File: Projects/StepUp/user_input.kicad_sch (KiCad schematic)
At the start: 3 parts, among them J15 Conn_02x03_Odd_Even

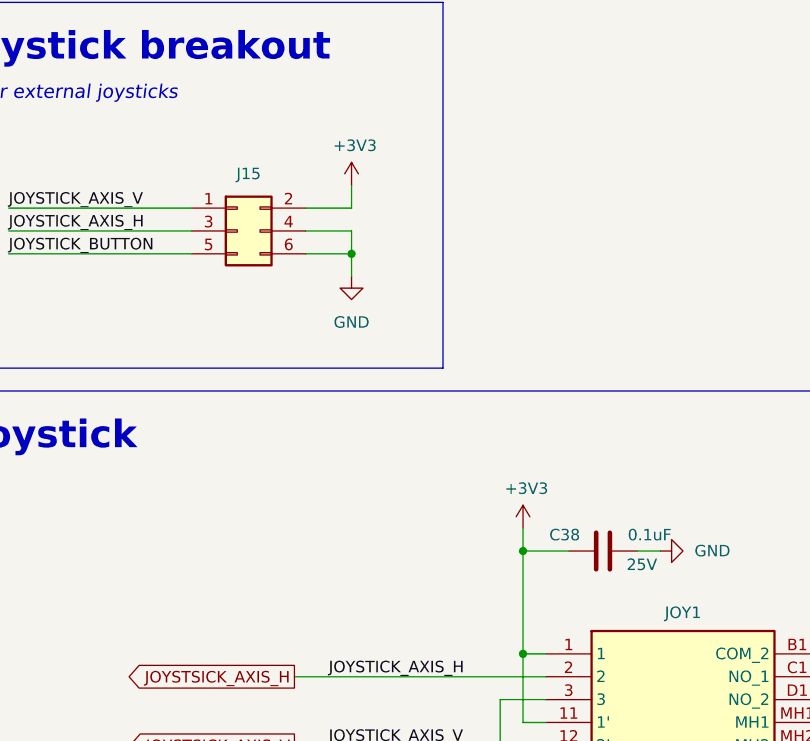
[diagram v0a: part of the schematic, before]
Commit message: feat(layout): TMC & Boost layout begin
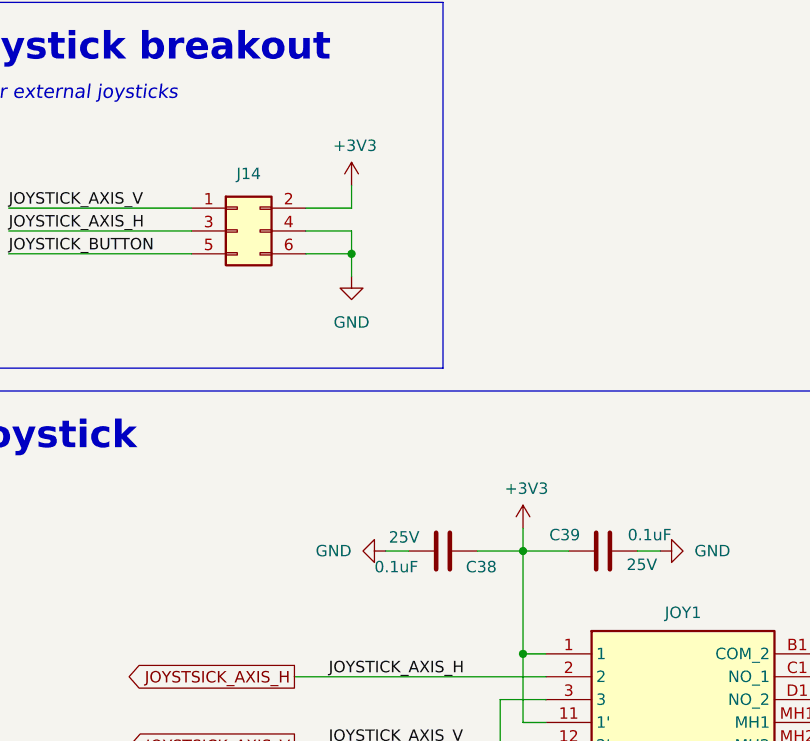
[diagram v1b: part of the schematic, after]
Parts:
- added C38: 0.1uF, Capacitor_SMD:C_0603_1608Metric, symbol Device:C
- renumbered C38 to C39, J15 to J14
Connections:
- net +3V3: now also C38.1
- net GND: now also C38.2
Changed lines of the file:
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@@
+	(wire
+		(pts
+			(xy 128.27 104.14) (xy 123.19 104.14)
+		)
+		(stroke
+			(width 0)
+			(type default)
+		)
+	)
 	(wire
 		(pts
@@
 		(pts
 			(xy 130.81 120.65) (xy 125.73 120.65)
+		)
+		(stroke
+			(width 0)
+			(type default)
+		)
+	)
+	(wire
+		(pts
+			(xy 115.57 104.14) (xy 113.03 104.14)
 		)
 		(stroke
@@
 	)
 	(symbol
+		(lib_id "power:GND")
+		(at 113.03 104.14 270)
+		(unit 1)
+		(exclude_from_sim no)
+		(in_bom yes)
+		(on_board yes)
+		(dnp no)
+		(fields_autoplaced yes)
+		(property "Reference" "#PWR0101"
+			(at 106.68 104.14 0)
+			(effects
+				(font
+					(size 1.27 1.27)
+				)
+				(hide yes)
+			)
+		)
+		(property "Value" "GND"
+			(at 109.22 104.1401 90)
+			(effects
+				(font
+					(size 1.27 1.27)
+				)
+				(justify right)
+			)
+		)
+		(property "Footprint" ""
+			(at 113.03 104.14 0)
+			(effects
+				(font
+					(size 1.27 1.27)
+				)
+				(hide yes)
+			)
+		)
+		(property "Datasheet" ""
+			(at 113.03 104.14 0)
+			(effects
+				(font
+					(size 1.27 1.27)
+				)
+				(hide yes)
+			)
+		)
+		(property "Description" "Power symbol creates a global label with name \"GND\" , ground"
+			(at 113.03 104.14 0)
+			(effects
+				(font
+					(size 1.27 1.27)
+				)
+				(hide yes)
+			)
+		)
+		(pin "1"
+		)
+		(instances
+			(project "StepUp"
+				(path "/e0cca1c7-c263-49eb-8c40-74000ebe5285/62dd6998-8b69-42c0-9c2f-b18953d44bc4"
+					(reference "#PWR0101")
+					(unit 1)
+				)
+			)
+		)
+	)
+	(symbol
 		(lib_id "Connector_Generic:Conn_02x03_Odd_Even")
 		(at 96.52 68.58 0)
@@
 		(dnp no)
 		(fields_autoplaced yes)
-		(property "Reference" "J15"
+		(property "Reference" "J14"
 			(at 97.79 62.23 0)
 			(effects
@@
 			(project "StepUp"
 				(path "/e0cca1c7-c263-49eb-8c40-74000ebe5285/62dd6998-8b69-42c0-9c2f-b18953d44bc4"
-					(reference "J15")
+					(reference "J14")
 					(unit 1)
 				)
@@
 		(dnp no)
 		(fields_autoplaced yes)
-		(property "Reference" "#PWR0101"
+		(property "Reference" "#PWR0100"
 			(at 109.22 80.01 0)
 			(effects
@@
 			(project "StepUp"
 				(path "/e0cca1c7-c263-49eb-8c40-74000ebe5285/62dd6998-8b69-42c0-9c2f-b18953d44bc4"
-					(reference "#PWR0101")
+					(reference "#PWR0100")
 					(unit 1)
 				)
@@
 		(on_board yes)
 		(dnp no)
-		(property "Reference" "C38"
+		(property "Reference" "C39"
 			(at 134.62 102.362 90)
 			(effects
@@
 			(project "StepUp"
 				(path "/e0cca1c7-c263-49eb-8c40-74000ebe5285/62dd6998-8b69-42c0-9c2f-b18953d44bc4"
-					(reference "C38")
+					(reference "C39")
 					(unit 1)
 				)
@@
 	)
 	(symbol
+		(lib_id "Device:C")
+		(at 119.38 104.14 270)
+		(unit 1)
+		(exclude_from_sim no)
+		(in_bom yes)
+		(on_board yes)
+		(dnp no)
+		(property "Reference" "C38"
+			(at 121.92 105.918 90)
+			(effects
+				(font
+					(size 1.27 1.27)
+				)
+				(justify left)
+			)
+		)
+		(property "Value" "0.1uF"
+			(at 111.76 105.918 90)
+			(effects
+				(font
+					(size 1.27 1.27)
+				)
+				(justify left)
+			)
+		)
+		(property "Footprint" "Capacitor_SMD:C_0603_1608Metric"
+			(at 115.57 105.1052 0)
+			(effects
+				(font
+					(size 1.27 1.27)
+				)
+				(hide yes)
+			)
+		)
+		(property "Datasheet" "~"
+			(at 119.38 104.14 0)
+			(effects
+				(font
+					(size 1.27 1.27)
+				)
+				(hide yes)
+			)
+		)
+		(property "Description" "Unpolarized capacitor"
+			(at 119.38 104.14 0)
+			(effects
+				(font
+					(size 1.27 1.27)
+				)
+				(hide yes)
+			)
+		)
+		(property "Voltage" "25V"
+			(at 115.062 102.616 90)
+			(effects
+				(font
+					(size 1.27 1.27)
+				)
+			)
+		)
+		(pin "2"
+		)
+		(pin "1"
+		)
+		(instances
+			(project "StepUp"
+				(path "/e0cca1c7-c263-49eb-8c40-74000ebe5285/62dd6998-8b69-42c0-9c2f-b18953d44bc4"
+					(reference "C38")
+					(unit 1)
+				)
+			)
+		)
+	)
+	(symbol
 		(lib_id "power:GND")
 		(at 125.73 134.62 0)
@@
 		(on_board yes)
 		(dnp no)
-		(property "Reference" "#PWR0100"
+		(property "Reference" "#PWR099"
 			(at 109.22 67.31 0)
 			(effects
@@
 			(project "StepUp"
 				(path "/e0cca1c7-c263-49eb-8c40-74000ebe5285/62dd6998-8b69-42c0-9c2f-b18953d44bc4"
-					(reference "#PWR0100")
+					(reference "#PWR099")
 					(unit 1)
 				)

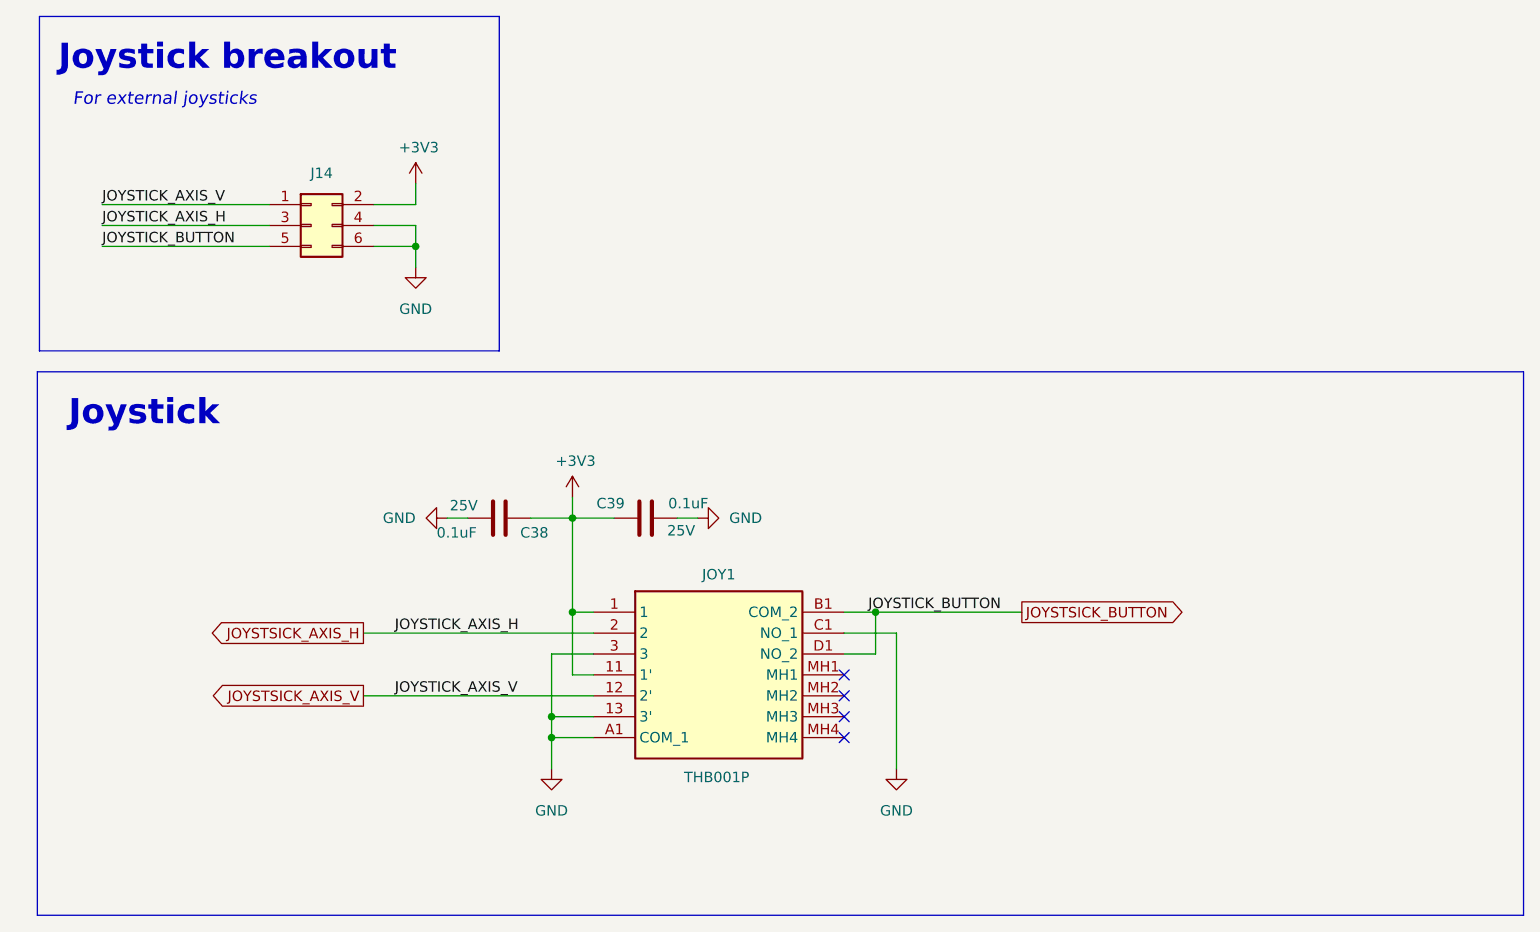
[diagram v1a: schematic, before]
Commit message: feat(layout): DRC ongoing, layout nearly complete
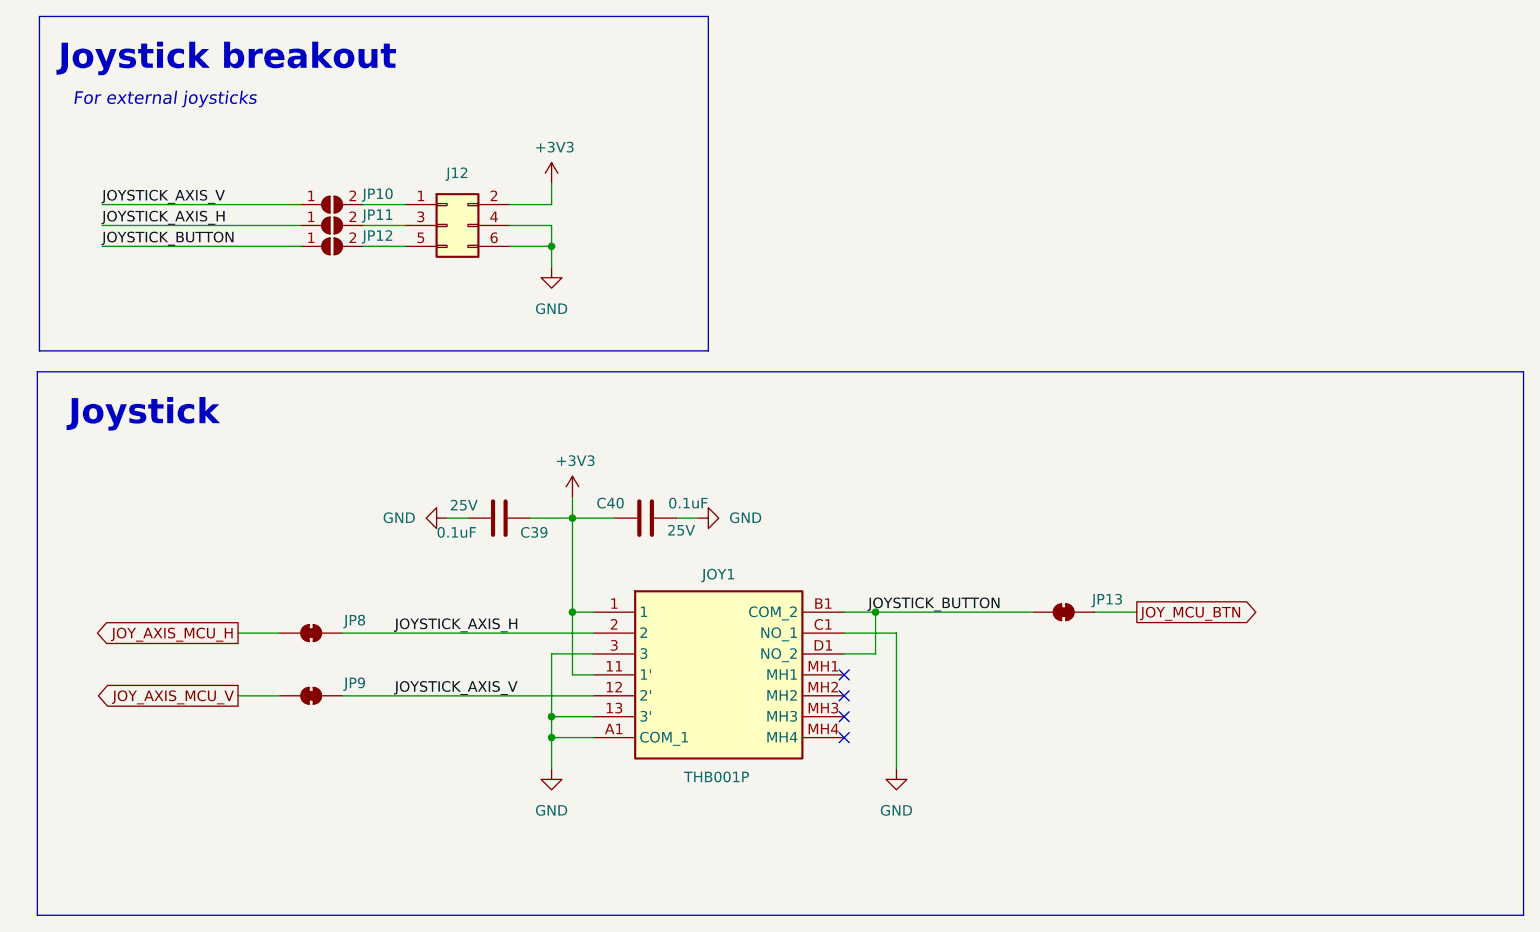
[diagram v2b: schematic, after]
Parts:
- added JP10, JP11, JP12: SolderJumper_2_Open, Jumper:SolderJumper-2_P1.3mm_Open_RoundedPad1.0x1.5mm, symbol Jumper:SolderJumper_2_Open
- added JP13, JP8, JP9: SolderJumper_2_Bridged, Jumper:SolderJumper-2_P1.3mm_Bridged2Bar_RoundedPad1.0x1.5mm, symbol Jumper:SolderJumper_2_Bridged
- renumbered C38 to C39, C39 to C40, J14 to J12
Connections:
- net JOYSTSICK_AXIS_H: no longer names the net of J12.3 (Pin_3)
- net JOYSTSICK_AXIS_H: now also JP11.2 (B); no longer JOY1.2
- net JOYSTSICK_AXIS_V: no longer names the net of J12.1 (Pin_1)
- net JOYSTSICK_AXIS_V: now also JP10.2 (B); no longer JOY1.12 (2')
- net JOYSTSICK_BUTTON renamed JOYSTICK_BUTTON
- net JOYSTICK_BUTTON: now also JP12.1 (A), JP13.1 (A); no longer J12.5 (Pin_5)
- new net: J12.5 (Pin_5), JP12.2 (B)
- new net JOYSTICK_AXIS_H: JOY1.2, JP11.1 (A), JP8.2 (B)
- new net JOYSTICK_AXIS_V: JOY1.12 (2'), JP10.1 (A), JP9.2 (B)
- new net JOY_AXIS_MCU_H: JP8.1 (A)
- new net JOY_AXIS_MCU_V: JP9.1 (A)
- new net JOY_MCU_BTN: JP13.2 (B)
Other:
- moved on the sheet: J12

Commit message: feat(StepUp): Release v0.1
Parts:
- C39, C40: Package (none) -> 0603; Type (none) -> SMD
- J12, JP10, JP11, JP12, JP13, JP8, JP9: now not fitted
- JOY1: MPN (none) -> THB001P; Manufacturer (none) -> C&K; Type (none) -> thru-hole
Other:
- company: Samio -> SJFOM
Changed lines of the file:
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@@
 		(title "User Input")
 		(date "2024-04-28")
-		(rev "v1.0")
-		(company "Samio")
+		(rev "v0.1")
+		(company "SJFOM")
 	)
 	(junction
@@
 		(dnp no)
 		(fields_autoplaced yes)
-		(property "Reference" "#PWR0111"
+		(property "Reference" "#PWR0113"
 			(at 106.68 104.14 0)
 			(effects
@@
 			(project "StepUp"
 				(path "/e0cca1c7-c263-49eb-8c40-74000ebe5285/62dd6998-8b69-42c0-9c2f-b18953d44bc4"
-					(reference "#PWR0111")
+					(reference "#PWR0113")
 					(unit 1)
 				)
@@
 		(in_bom yes)
 		(on_board yes)
-		(dnp no)
+		(dnp yes)
 		(fields_autoplaced yes)
 		(property "Reference" "J12"
@@
 		)
 		(property "Description" "Generic connector, double row, 02x03, odd/even pin numbering scheme (row 1 odd numbers, row 2 even numbers), script generated (kicad-library-utils/schlib/autogen/connector/)"
+			(at 113.03 68.58 0)
+			(effects
+				(font
+					(size 1.27 1.27)
+				)
+				(hide yes)
+			)
+		)
+		(property "Type" ""
 			(at 113.03 68.58 0)
 			(effects
@@
 		(dnp no)
 		(fields_autoplaced yes)
-		(property "Reference" "#PWR0113"
+		(property "Reference" "#PWR0115"
 			(at 125.73 80.01 0)
 			(effects
@@
 			(project "StepUp"
 				(path "/e0cca1c7-c263-49eb-8c40-74000ebe5285/62dd6998-8b69-42c0-9c2f-b18953d44bc4"
-					(reference "#PWR0113")
+					(reference "#PWR0115")
 					(unit 1)
 				)
@@
 		(in_bom yes)
 		(on_board yes)
-		(dnp no)
+		(dnp yes)
 		(property "Reference" "JP10"
 			(at 104.648 64.77 0)
@@
 		)
 		(property "Description" "Solder Jumper, 2-pole, open"
+			(at 99.06 66.04 0)
+			(effects
+				(font
+					(size 1.27 1.27)
+				)
+				(hide yes)
+			)
+		)
+		(property "Type" ""
 			(at 99.06 66.04 0)
 			(effects
@@
 			)
 		)
+		(property "Type" "SMD"
+			(at 137.16 104.14 0)
+			(effects
+				(font
+					(size 1.27 1.27)
+				)
+				(hide yes)
+			)
+		)
+		(property "Package" "0603"
+			(at 137.16 104.14 0)
+			(effects
+				(font
+					(size 1.27 1.27)
+				)
+				(hide yes)
+			)
+		)
 		(pin "2"
 		)
@@
 		(in_bom no)
 		(on_board yes)
-		(dnp no)
+		(dnp yes)
 		(property "Reference" "JP9"
 			(at 101.854 124.206 0)
@@
 		)
 		(property "Description" "Solder Jumper, 2-pole, closed/bridged"
+			(at 96.52 125.73 0)
+			(effects
+				(font
+					(size 1.27 1.27)
+				)
+				(hide yes)
+			)
+		)
+		(property "Type" ""
 			(at 96.52 125.73 0)
 			(effects
@@
 		(in_bom yes)
 		(on_board yes)
-		(dnp no)
+		(dnp yes)
 		(property "Reference" "JP12"
 			(at 104.648 69.85 0)
@@
 		)
 		(property "Description" "Solder Jumper, 2-pole, open"
+			(at 99.06 71.12 0)
+			(effects
+				(font
+					(size 1.27 1.27)
+				)
+				(hide yes)
+			)
+		)
+		(property "Type" ""
 			(at 99.06 71.12 0)
 			(effects
@@
 		(in_bom yes)
 		(on_board yes)
-		(dnp no)
+		(dnp yes)
 		(property "Reference" "JP11"
 			(at 104.648 67.31 0)
@@
 		)
 		(property "Description" "Solder Jumper, 2-pole, open"
+			(at 99.06 68.58 0)
+			(effects
+				(font
+					(size 1.27 1.27)
+				)
+				(hide yes)
+			)
+		)
+		(property "Type" ""
 			(at 99.06 68.58 0)
 			(effects
@@
 			)
 		)
+		(property "MPN" "THB001P"
+			(at 130.81 115.57 0)
+			(effects
+				(font
+					(size 1.27 1.27)
+				)
+				(hide yes)
+			)
+		)
+		(property "Manufacturer" "C&K"
+			(at 130.81 115.57 0)
+			(effects
+				(font
+					(size 1.27 1.27)
+				)
+				(hide yes)
+			)
+		)
+		(property "Type" "thru-hole"
+			(at 130.81 115.57 0)
+			(effects
+				(font
+					(size 1.27 1.27)
+				)
+				(hide yes)
+			)
+		)
 		(pin "12"
 		)
@@
 		(dnp no)
 		(fields_autoplaced yes)
-		(property "Reference" "#PWR0117"
+		(property "Reference" "#PWR0119"
 			(at 167.64 140.97 0)
 			(effects
@@
 			(project "StepUp"
 				(path "/e0cca1c7-c263-49eb-8c40-74000ebe5285/62dd6998-8b69-42c0-9c2f-b18953d44bc4"
-					(reference "#PWR0117")
+					(reference "#PWR0119")
 					(unit 1)
 				)
@@
 		(dnp no)
 		(fields_autoplaced yes)
-		(property "Reference" "#PWR0116"
+		(property "Reference" "#PWR0118"
 			(at 149.86 104.14 0)
 			(effects
@@
 			(project "StepUp"
 				(path "/e0cca1c7-c263-49eb-8c40-74000ebe5285/62dd6998-8b69-42c0-9c2f-b18953d44bc4"
-					(reference "#PWR0116")
+					(reference "#PWR0118")
 					(unit 1)
 				)
@@
 		(in_bom no)
 		(on_board yes)
-		(dnp no)
+		(dnp yes)
 		(property "Reference" "JP8"
 			(at 101.854 116.586 0)
@@
 		)
 		(property "Description" "Solder Jumper, 2-pole, closed/bridged"
+			(at 96.52 118.11 0)
+			(effects
+				(font
+					(size 1.27 1.27)
+				)
+				(hide yes)
+			)
+		)
+		(property "Type" ""
 			(at 96.52 118.11 0)
 			(effects
@@
 			)
 		)
+		(property "Type" "SMD"
+			(at 119.38 104.14 0)
+			(effects
+				(font
+					(size 1.27 1.27)
+				)
+				(hide yes)
+			)
+		)
+		(property "Package" "0603"
+			(at 119.38 104.14 0)
+			(effects
+				(font
+					(size 1.27 1.27)
+				)
+				(hide yes)
+			)
+		)
 		(pin "2"
 		)
@@
 		(dnp no)
 		(fields_autoplaced yes)
-		(property "Reference" "#PWR0114"
+		(property "Reference" "#PWR0116"
 			(at 125.73 140.97 0)
 			(effects
@@
 			(project "StepUp"
 				(path "/e0cca1c7-c263-49eb-8c40-74000ebe5285/62dd6998-8b69-42c0-9c2f-b18953d44bc4"
-					(reference "#PWR0114")
+					(reference "#PWR0116")
 					(unit 1)
 				)
@@
 		(on_board yes)
 		(dnp no)
-		(property "Reference" "#PWR0112"
+		(property "Reference" "#PWR0114"
 			(at 125.73 67.31 0)
 			(effects
@@
 			(project "StepUp"
 				(path "/e0cca1c7-c263-49eb-8c40-74000ebe5285/62dd6998-8b69-42c0-9c2f-b18953d44bc4"
-					(reference "#PWR0112")
+					(reference "#PWR0114")
 					(unit 1)
 				)
@@
 		(in_bom no)
 		(on_board yes)
-		(dnp no)
+		(dnp yes)
 		(property "Reference" "JP13"
 			(at 193.294 114.046 0)
@@
 		)
 		(property "Description" "Solder Jumper, 2-pole, closed/bridged"
+			(at 187.96 115.57 0)
+			(effects
+				(font
+					(size 1.27 1.27)
+				)
+				(hide yes)
+			)
+		)
+		(property "Type" ""
 			(at 187.96 115.57 0)
 			(effects
@@
 		(on_board yes)
 		(dnp no)
-		(property "Reference" "#PWR0115"
+		(property "Reference" "#PWR0117"
 			(at 128.27 105.41 0)
 			(effects
@@
 			(project "StepUp"
 				(path "/e0cca1c7-c263-49eb-8c40-74000ebe5285/62dd6998-8b69-42c0-9c2f-b18953d44bc4"
-					(reference "#PWR0115")
+					(reference "#PWR0117")
 					(unit 1)
 				)

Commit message: chore(bom): Update from PCB BoM
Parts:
- C39, C40: Dielectric (none) -> X7R; MPN (none) -> CC0603KRX7R8BB104; Manufacturer (none) -> YAGEO; Tolerance (none) -> 10%
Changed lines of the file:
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@@
+			)
+		)
+		(property "Dielectric" "X7R"
+			(at 137.16 104.14 0)
+			(effects
+				(font
+					(size 1.27 1.27)
+				)
+				(hide yes)
+			)
+		)
+		(property "MPN" "CC0603KRX7R8BB104"
+			(at 137.16 104.14 0)
+			(effects
+				(font
+					(size 1.27 1.27)
+				)
+				(hide yes)
+			)
+		)
+		(property "Manufacturer" "YAGEO"
+			(at 137.16 104.14 0)
+			(effects
+				(font
+					(size 1.27 1.27)
+				)
+				(hide yes)
+			)
+		)
+		(property "Tolerance" "10%"
+			(at 137.16 104.14 0)
+			(effects
+				(font
+					(size 1.27 1.27)
+				)
+				(hide yes)
 			)
 		)
@@
 			(at 119.38 104.14 0)
 			(effects
+				(font
+					(size 1.27 1.27)
+				)
+				(hide yes)
+			)
+		)
+		(property "Dielectric" "X7R"
+			(at 119.38 104.14 0)
+			(effects
+				(font
+					(size 1.27 1.27)
+				)
+				(hide yes)
+			)
+		)
+		(property "MPN" "CC0603KRX7R8BB104"
+			(at 119.38 104.14 0)
+			(effects
+				(font
+					(size 1.27 1.27)
+				)
+				(hide yes)
+			)
+		)
+		(property "Manufacturer" "YAGEO"
+			(at 119.38 104.14 0)
+			(effects
+				(font
+					(size 1.27 1.27)
+				)
+				(hide yes)
+			)
+		)
+		(property "Tolerance" "10%"
+			(at 119.38 104.14 0)
+			(effects
